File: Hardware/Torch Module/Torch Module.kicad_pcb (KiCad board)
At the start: 2 copper layers, 124 x 71.8 mm, 82 parts, among them J1 Torch, J10 Module conn, J11 Conn_01x18_Male, J12 Conn_01x02_Male, J14 Conn_01x02_Male, J15 Module conn, J16 Reset, J17 Reset, J18 Reset, J2 Module3, J3 Conn_01x18_Male, J4 Limit, J6 8P8C_LED_Shielded, J7 Module1, J8 Torch, J9 2.54 pin, K1 G6E, Q1 IRLML2402, Q2 IRLML2402, Q3 IRLML2402, Q4 IRLML2402, Q5 IRLML2402, U1 ULN2002, U2 NCV8114ASN150T1G, U3 ADS1115IDGS

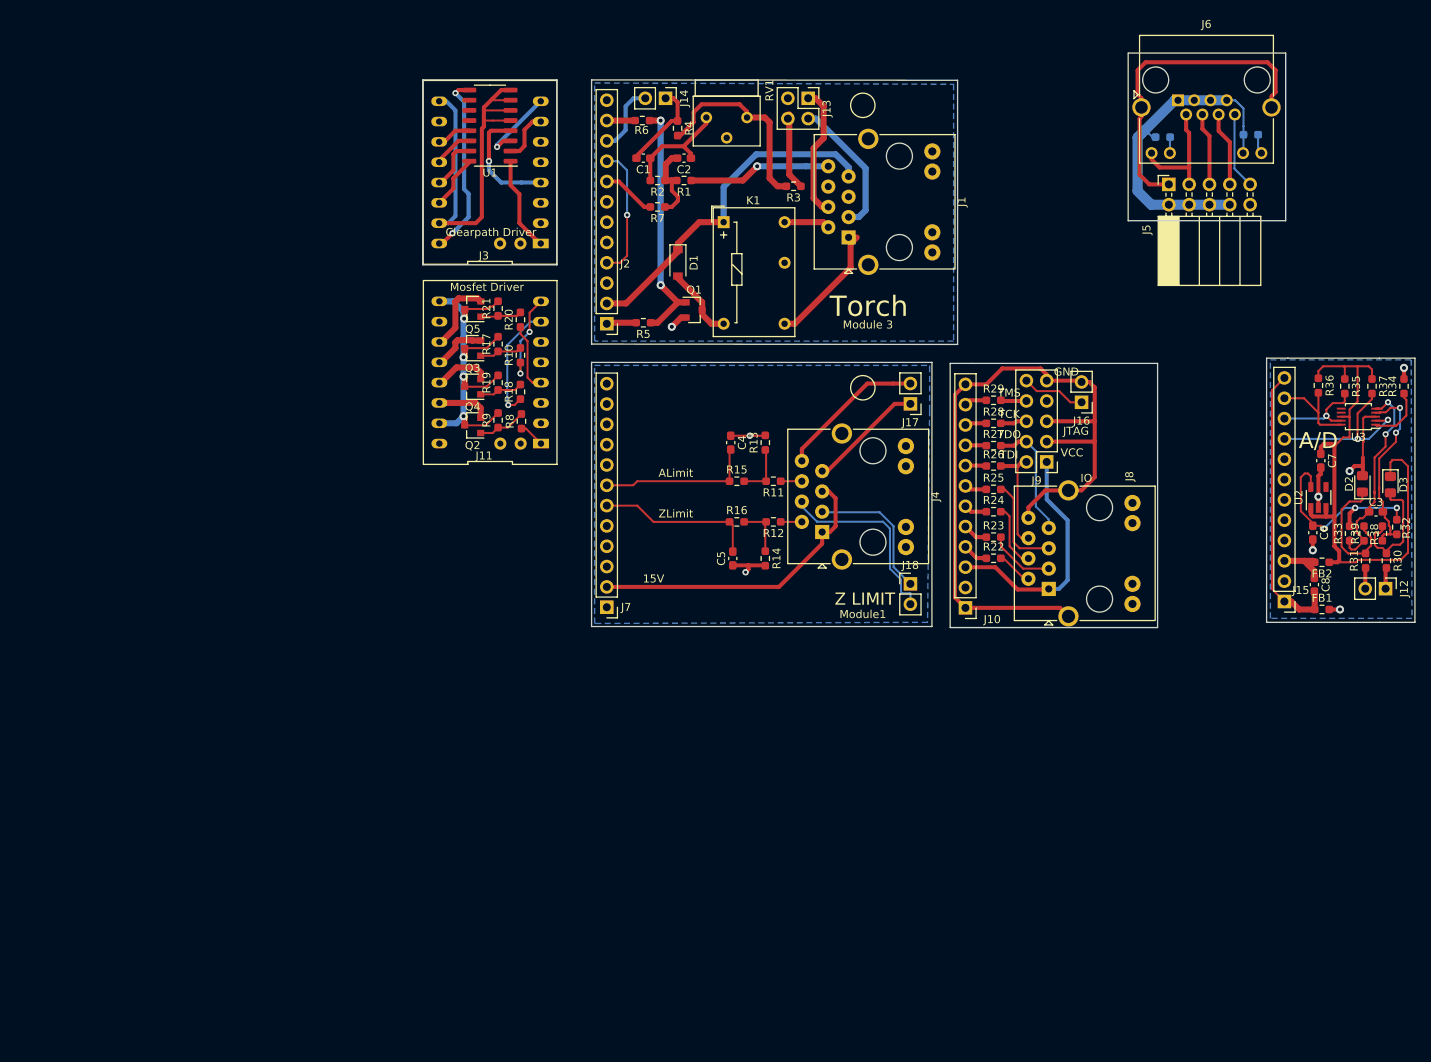
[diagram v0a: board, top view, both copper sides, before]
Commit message: Ordered parts, finished modules, fixed rj45
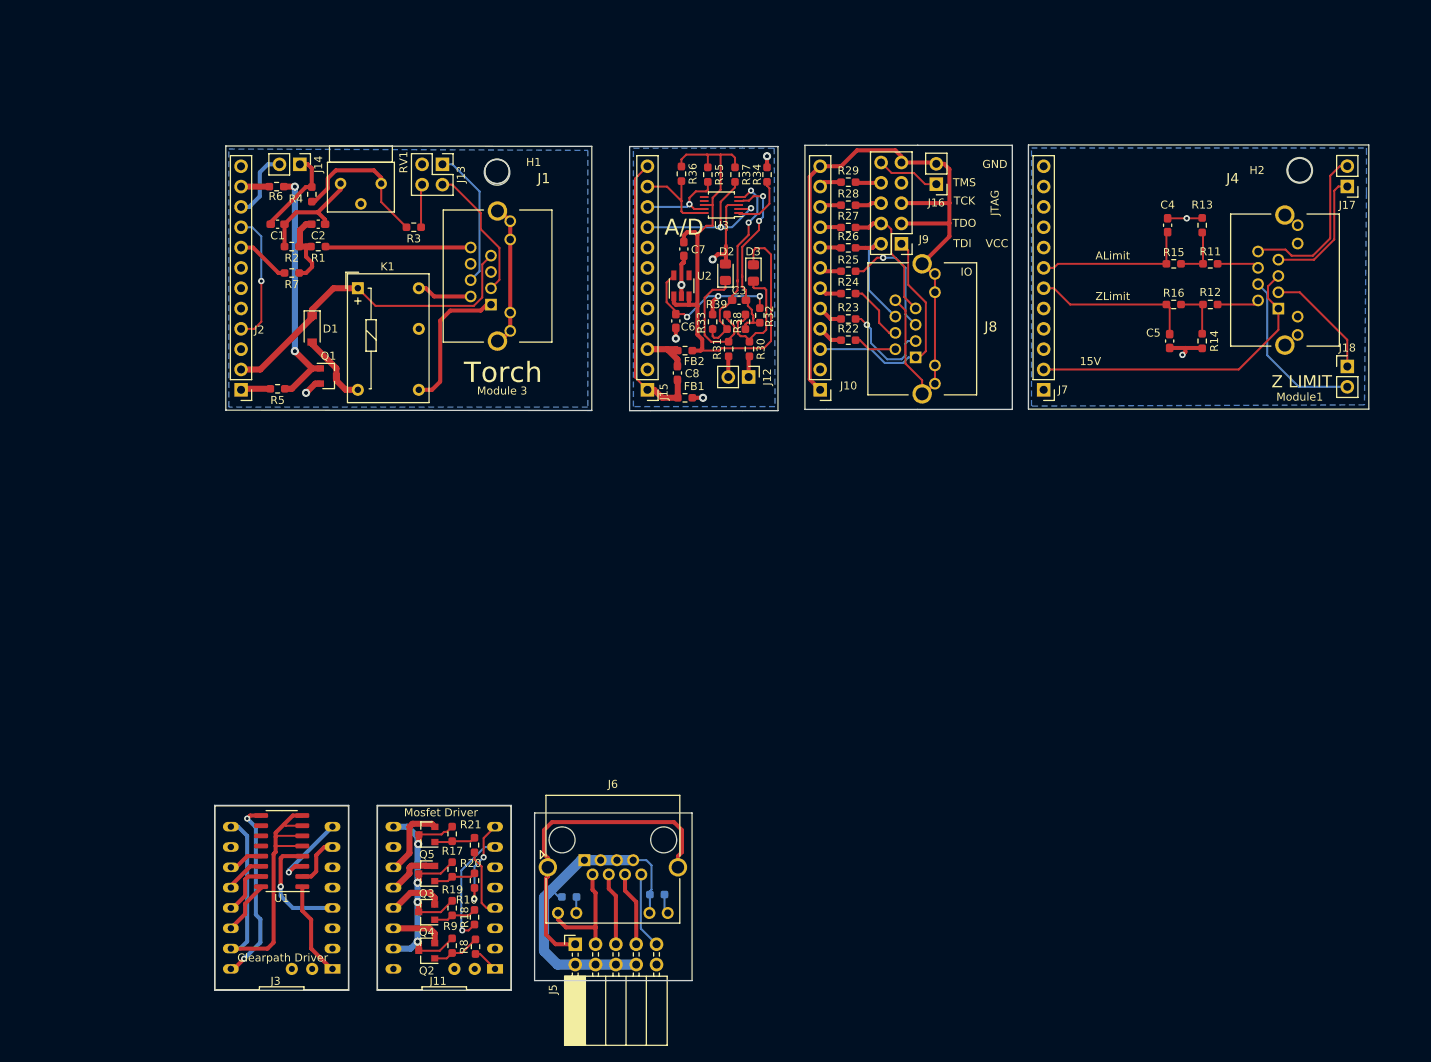
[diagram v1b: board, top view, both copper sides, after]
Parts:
- added H1: MountingHole, MountingHole:MountingHole_3.2mm_M3, F.Cu at (106.9, 64.3)
- added H2: MountingHole, MountingHole:MountingHole_3.2mm_M3, F.Cu at (207.3, 64.0)
- J1, J4, J8: footprint Connector_RJ:RJ45_BEL_SS74301-00x_Vertical -> RJHSE-3380:RJHSE3384
- moved J6 120.5 mm to (117.8, 150.2)
- moved R40 120.5 mm to (126.9, 154.5)
- moved R41 120.5 mm to (115.9, 154.8)
- moved J5 120.5 mm to (116.7, 160.7)
- moved U1 94.3 mm to (80.0, 149.1)
- moved J3 94.3 mm to (80.0, 154.9)
- moved C3 83.9 mm to (137.2, 80.2)
- moved C6 83.9 mm to (129.3, 82.8)
- moved C7 83.9 mm to (130.3, 73.8)
- moved FB1 83.9 mm to (130.4, 92.4)
- moved FB2 83.9 mm to (130.4, 86.5)
- moved R32 83.9 mm to (139.8, 82.1)
- moved R34 83.9 mm to (140.7, 64.5)
- moved R35 83.9 mm to (133.3, 64.5)
- moved R37 83.9 mm to (136.7, 64.5)
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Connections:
- J1 pad 10: (no net) -> Net-(C1-Pad1)
- J1 pad 11: (no net) -> Net-(C1-Pad1)
- J1 pad 12: (no net) -> Net-(C1-Pad1)
- J1 pad 5: (no net) -> Net-(J1-Pad5)
- J1 pad 6: (no net) -> Net-(J1-Pad6)
- J1 pad 9: (no net) -> Net-(C1-Pad1)
- J10 pad 2: (no net) -> Net-(J10-Pad2)
- J11 pad 10: (no net) -> Net-(J11-Pad10)
- J11 pad 16: (no net) -> Net-(J11-Pad16)
- J11 pad 17: (no net) -> Net-(J11-Pad17)
- J11 pad 18: (no net) -> Net-(J11-Pad18)
- J11 pad 2: (no net) -> Net-(J11-Pad2)
- J11 pad 3: (no net) -> Net-(J11-Pad3)
- J11 pad 5: (no net) -> Net-(J11-Pad5)
- J11 pad 6: (no net) -> Net-(J11-Pad6)
- J15 pad 2: (no net) -> Net-(J15-Pad2)
- J15 pad 4: (no net) -> Net-(J15-Pad4)
- J15 pad 5: (no net) -> Net-(J15-Pad5)
- J15 pad 6: (no net) -> Net-(J15-Pad6)
- J15 pad 7: (no net) -> Net-(J15-Pad7)
- J15 pad 8: (no net) -> Net-(J15-Pad8)
- J2 pad 3: (no net) -> Net-(J2-Pad3)
- J2 pad 5: (no net) -> Net-(J2-Pad5)
- J2 pad 6: (no net) -> Net-(J2-Pad6)
- J2 pad 7: (no net) -> Net-(J2-Pad7)
- J3 pad 10: (no net) -> Net-(J3-Pad10)
- J3 pad 17: (no net) -> Net-(J3-Pad17)
- J3 pad 18: (no net) -> Net-(J3-Pad18)
- J3 pad 2: (no net) -> Net-(J3-Pad2)
- J3 pad 3: (no net) -> Net-(J3-Pad3)
- J3 pad 5: (no net) -> Net-(J3-Pad5)
- J3 pad 6: (no net) -> Net-(J3-Pad6)
- J4 pad 10: (no net) -> Net-(C4-Pad1)
- J4 pad 11: (no net) -> Net-(C4-Pad1)
- J4 pad 12: (no net) -> Net-(C4-Pad1)
- J4 pad 9: (no net) -> Net-(C4-Pad1)
- J5 pad 10: (no net) -> Net-(J5-Pad10)
- J7 pad 10: (no net) -> Net-(J7-Pad10)
- J7 pad 11: (no net) -> Net-(J7-Pad11)
- J7 pad 3: (no net) -> Net-(J7-Pad3)
- J7 pad 4: (no net) -> Net-(J7-Pad4)
- J7 pad 5: (no net) -> Net-(J7-Pad5)
- J7 pad 8: (no net) -> Net-(J7-Pad8)
- J7 pad 9: (no net) -> Net-(J7-Pad9)
- J8 pad 10: (no net) -> Net-(J10-Pad1)
- J8 pad 11: (no net) -> Net-(J10-Pad1)
- J8 pad 12: (no net) -> Net-(J10-Pad1)
- J8 pad 9: (no net) -> Net-(J10-Pad1)
- J9 pad 7: (no net) -> Net-(J9-Pad7)
- K1 pad 10: (no net) -> Net-(K1-Pad10)
- U1 pad 10: (no net) -> Net-(U1-Pad10)
- U1 pad 11: (no net) -> Net-(U1-Pad11)
- U1 pad 12: (no net) -> Net-(U1-Pad12)
- U2 pad 4: (no net) -> Net-(U2-Pad4)
- U3 pad 6: (no net) -> Net-(U3-Pad6)
- U3 pad 7: (no net) -> Net-(U3-Pad7)
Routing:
- net Net-(C1-Pad1): track 20.2 -> 38.2 mm
- net Net-(J10-Pad1): track 95.5 -> 104.1 mm
- net Net-(R3-Pad2): track 24.7 -> 18.9 mm
- net Net-(J13-Pad4): track 9.60 -> 5.38 mm
- net Net-(C6-Pad1): track 25.4 -> 21.5 mm
- net Net-(J8-Pad3): track 8.82 -> 12.4 mm, vias 0 -> 1
- net Net-(J18-Pad1): track 17.7 -> 14.4 mm
- net Net-(J18-Pad2): track 23.9 -> 21.0 mm
- net Net-(J8-Pad5): track 12.2 -> 15.1 mm, vias 0 -> 1
- net Net-(J4-Pad2): track 2.64 -> 5.26 mm
- net Net-(J1-Pad1): track 15.3 -> 17.9 mm
- net Net-(J4-Pad6): track 2.64 -> 5.26 mm
- net Net-(J17-Pad2): track 18.4 -> 20.8 mm
- net Net-(J17-Pad1): track 14.5 -> 16.0 mm
- net Net-(J1-Pad2): track 5.72 -> 6.91 mm
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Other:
- board size 124 x 71.8 mm -> 144.3 x 105.7 mm
- board text added: "x1 Per Panel"
- board text added: "x4 Per Panel"

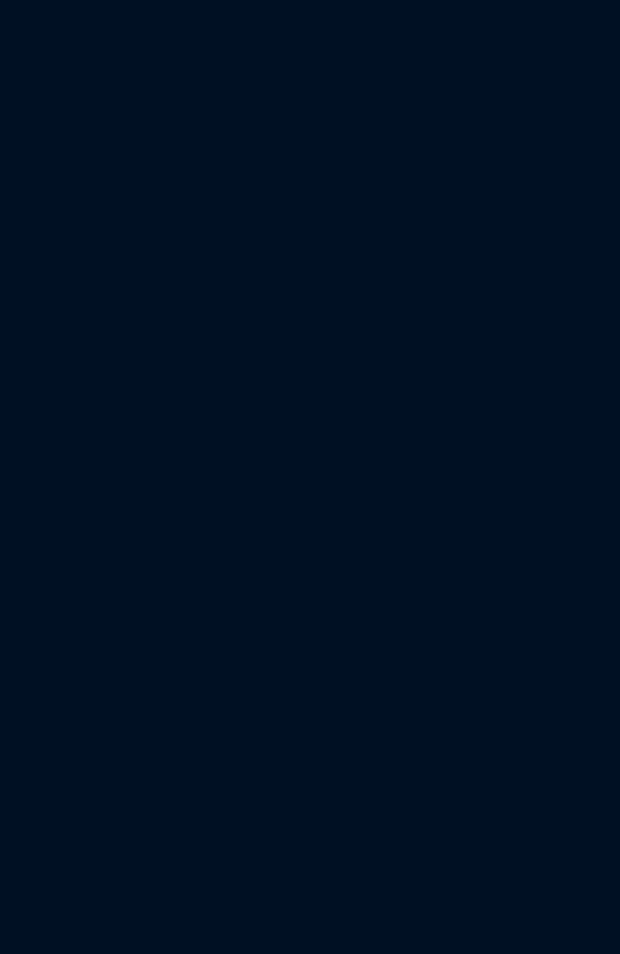
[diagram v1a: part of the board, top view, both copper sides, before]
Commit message: Added RJ45 Clearpath BOB, minor torch module footprint fix
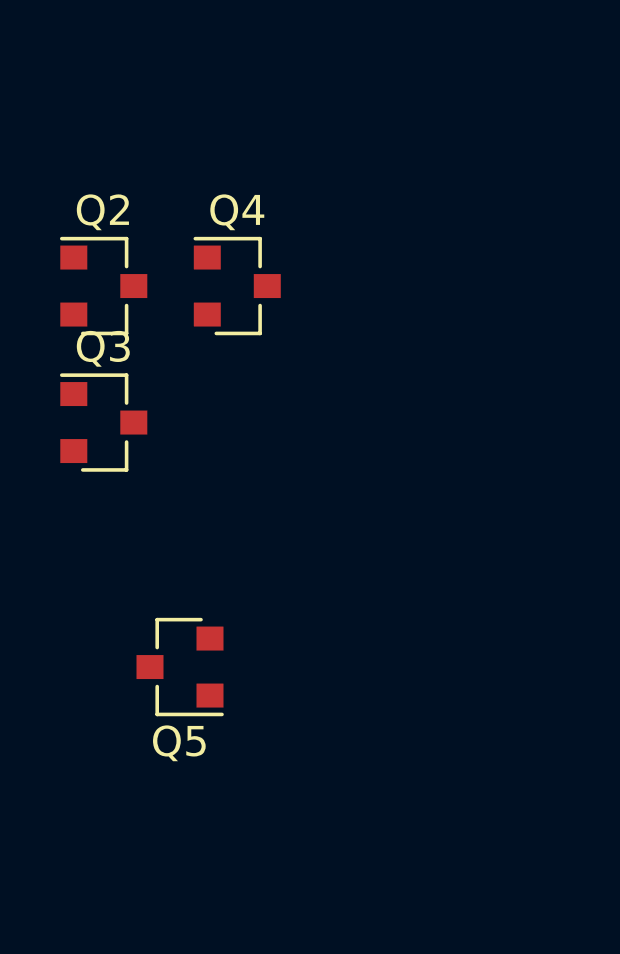
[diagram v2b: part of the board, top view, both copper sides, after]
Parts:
- added Q2: IRLML2402, Package_TO_SOT_SMD:SOT-23, F.Cu at (48.3, 142.2)
- added Q3: IRLML2402, Package_TO_SOT_SMD:SOT-23, F.Cu at (48.3, 146.8)
- added Q4: IRLML2402, Package_TO_SOT_SMD:SOT-23, F.Cu at (52.7, 142.2)
- added Q5: IRLML2402, Package_TO_SOT_SMD:SOT-23, F.Cu at (50.8, 154.9)
